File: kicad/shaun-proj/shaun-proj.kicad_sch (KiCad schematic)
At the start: 51 parts, among them J1 USB_C_Receptacle_USB2.0_16P, J2 Conn_02x16_Odd_Even, J3 Conn_01x02_Socket, Q1 AO3401A, Q2 AO3400A, U1 CH224K, U2 TPS5430DDA, U3 INA219AxD, U5 TP4056-42-ESOP8

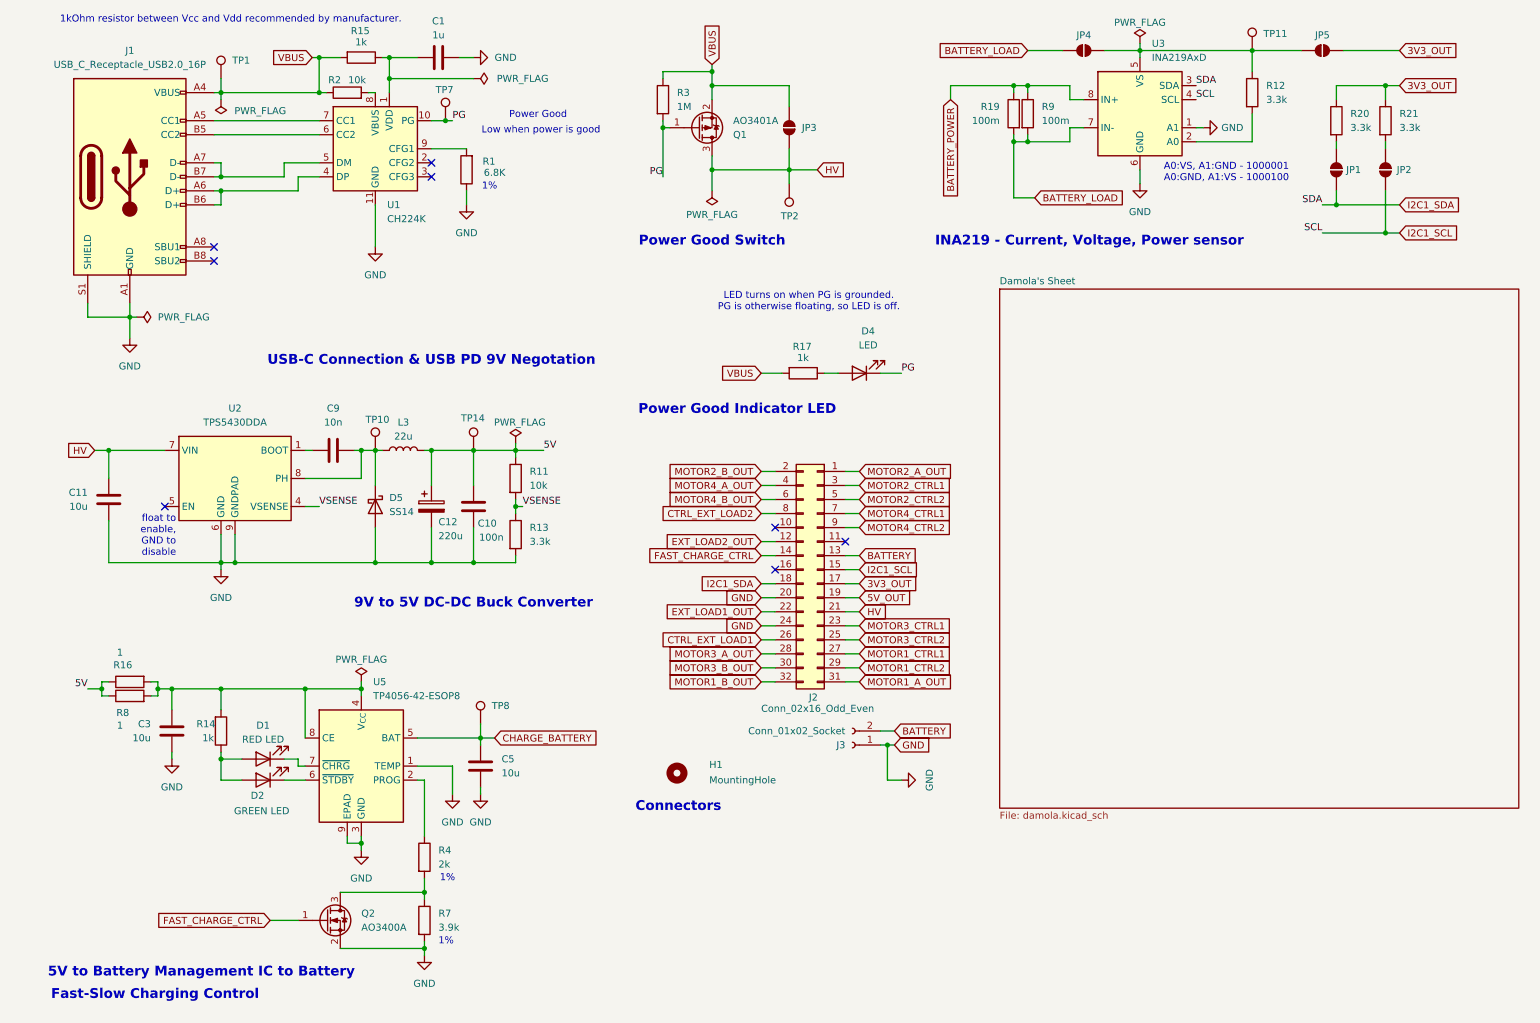
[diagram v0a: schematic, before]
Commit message: improved schematic, included more comments
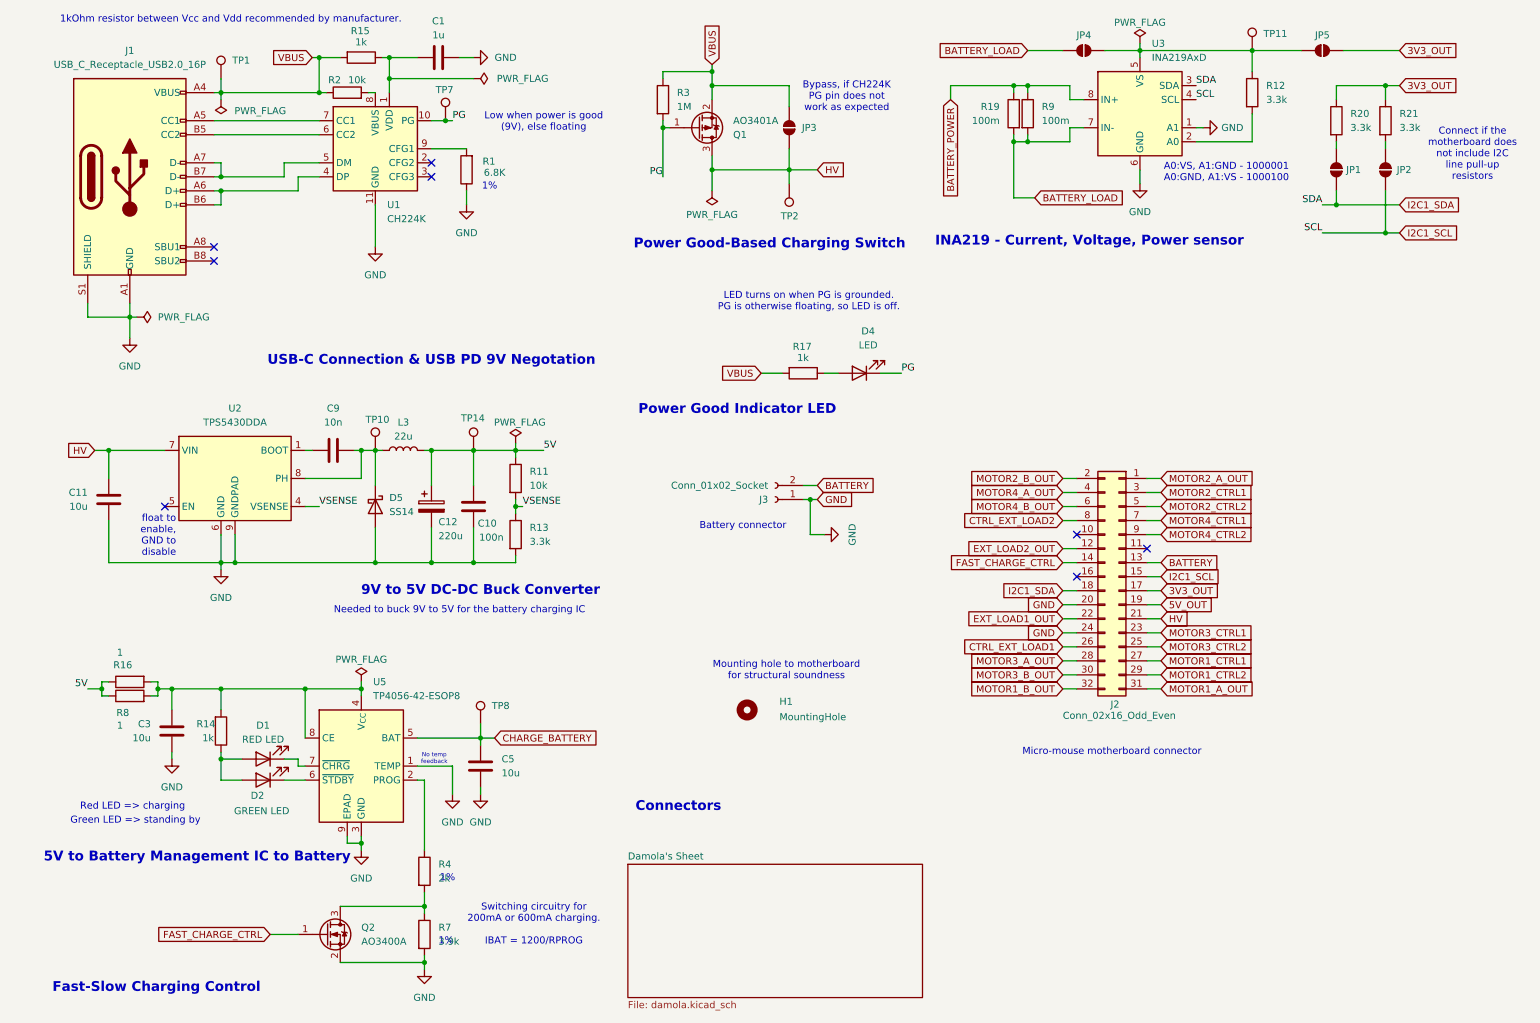
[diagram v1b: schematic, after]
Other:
- note added: "Battery connector"
- note added: "Bypass, if CH224K PG pin does not work as expected"
- note added: "Connect if the motherboard does not include I2C line pull-up resistors"
- note added: "Green LED => standing by"
- note added: "Low when power is good (9V), else floating"
- note added: "Micro-mouse motherboard connector"
- note added: "Mounting hole to motherboard for structural soundness"
- note added: "Needed to buck 9V to 5V for the battery charging IC"
- note added: "No temp feedback"
- note added: "Power Good-Based Charging Switch"
- note added: "Red LED => charging"
- note added: "Switching circuitry for 200mA or 600mA charging. IBAT = 1200/RPROG"
- note removed: "Low when power is good"
- note removed: "Power Good"
- note removed: "Power Good Switch"
- moved on the sheet: H1, J2, J3, Q2, R4, R7
